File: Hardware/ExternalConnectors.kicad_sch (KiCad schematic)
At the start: 5 parts, among them J2 FTSH-105-X-X-DV-007-P-X, P1 USB_C_Plug_USB2.0

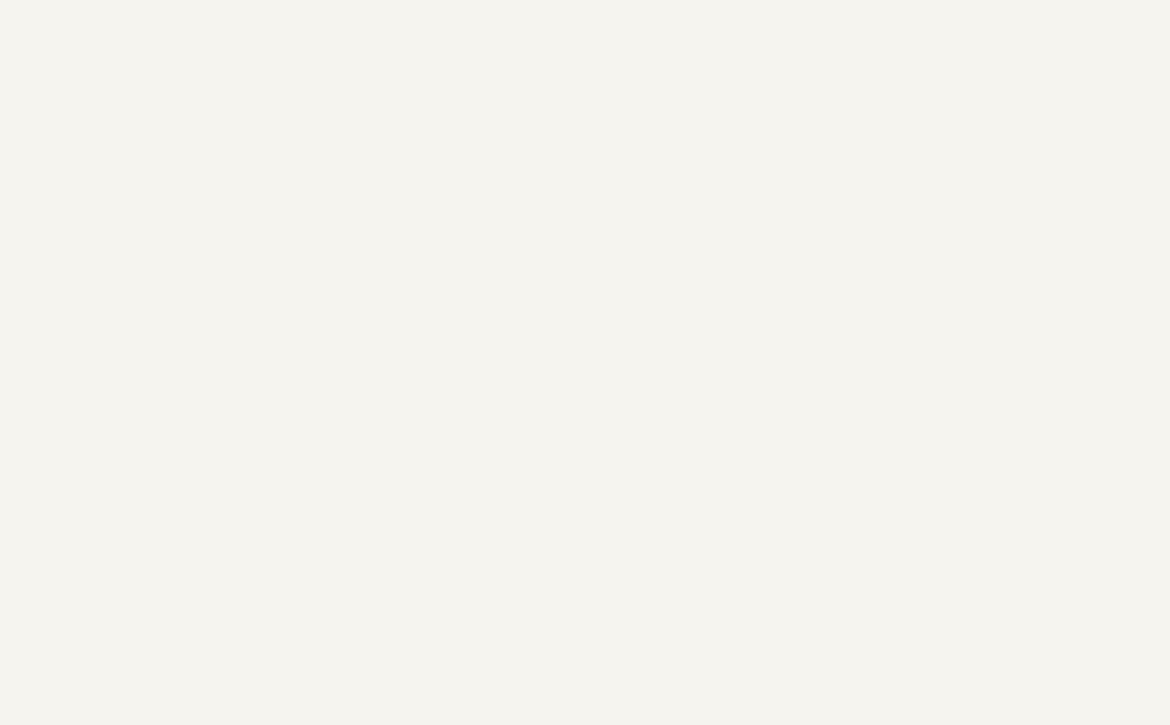
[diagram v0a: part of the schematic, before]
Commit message: shutdown pin connection to RF chain
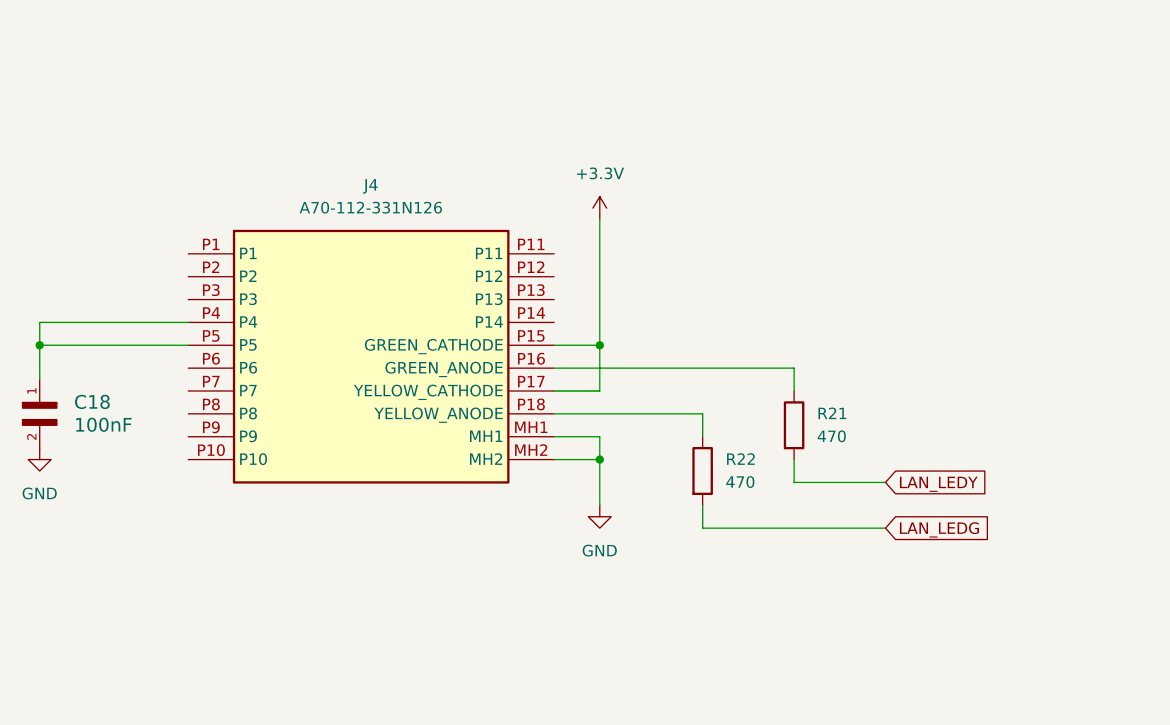
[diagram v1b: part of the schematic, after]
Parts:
- added C18: 100nF, C0402C104J8RACTU:CAPC10555_55N_KEM-L, symbol 2025-06-22_21-59-05:C0402C104J8RACTU
- added J4: A70-112-331N126, A70-112-331N126:A70112331N126, symbol A70-112-331N126:A70-112-331N126
- added R21, R22: 470, Resistor_SMD:R_0402_1005Metric, symbol Device:R
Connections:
- net +3.3V: now also J4.P15 (GREEN_CATHODE), J4.P17 (YELLOW_CATHODE)
- net GND: now also C18.2, J4.MH1, J4.MH2
- new net: J4.P16 (GREEN_ANODE), R21.1
- new net: J4.P18 (YELLOW_ANODE), R22.1
- new net: C18.1, J4.P4, J4.P5
- new net LAN_LEDG: R22.2
- new net LAN_LEDY: R21.2
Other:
- company: (none) -> Thomas Montano
- title: (none) -> External Connections
